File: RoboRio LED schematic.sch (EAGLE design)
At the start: 5 parts

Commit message: Jordan - RoboRio LED fixed
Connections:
- removed net 6V: R1.2, ROBORIO_PWM.2
- removed net N$3: D2.A, R2.1
- new net N$2: R1.2
- new net N$4: D2.A, R2.2
- net N$1: now also ROBORIO_PWM.2; no longer D1.A
- net S: now also R2.1; no longer R2.2
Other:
- moved on the sheet: R1, R2
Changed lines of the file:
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@@
 <instance part="D1" gate="G$1" x="-12.7" y="60.96" rot="R90"/>
 <instance part="D2" gate="G$1" x="20.32" y="60.96" rot="R90"/>
-<instance part="R1" gate="G$1" x="-27.94" y="60.96" rot="R180"/>
-<instance part="R2" gate="G$1" x="5.08" y="60.96" rot="R180"/>
+<instance part="R1" gate="G$1" x="-27.94" y="60.96"/>
+<instance part="R2" gate="G$1" x="5.08" y="60.96"/>
 </instances>
 <busses>
 </busses>
 <nets>
-<net name="N$1" class="0">
-<segment>
-<pinref part="R1" gate="G$1" pin="1"/>
-<pinref part="D1" gate="G$1" pin="A"/>
-<wire x1="-22.86" y1="60.96" x2="-15.24" y2="60.96" width="0.1524" layer="91"/>
-</segment>
-</net>
 <net name="S" class="0">
 <segment>
-<pinref part="D1" gate="G$1" pin="C"/>
-<pinref part="R2" gate="G$1" pin="2"/>
-<wire x1="-7.62" y1="60.96" x2="-5.08" y2="60.96" width="0.1524" layer="91"/>
 <pinref part="ROBORIO_PWM" gate="J$1" pin="3"/>
-<wire x1="-5.08" y1="60.96" x2="0" y2="60.96" width="0.1524" layer="91"/>
 <wire x1="-45.72" y1="63.5" x2="-45.72" y2="68.58" width="0.1524" layer="91"/>
 <wire x1="-45.72" y1="68.58" x2="-5.08" y2="68.58" width="0.1524" layer="91"/>
+<pinref part="D1" gate="G$1" pin="C"/>
+<pinref part="R2" gate="G$1" pin="1"/>
+<wire x1="-7.62" y1="60.96" x2="-5.08" y2="60.96" width="0.1524" layer="91"/>
+<wire x1="-5.08" y1="60.96" x2="0" y2="60.96" width="0.1524" layer="91"/>
 <wire x1="-5.08" y1="68.58" x2="-5.08" y2="60.96" width="0.1524" layer="91"/>
 <junction x="-5.08" y="60.96"/>
-</segment>
-</net>
-<net name="N$3" class="0">
-<segment>
-<pinref part="R2" gate="G$1" pin="1"/>
-<pinref part="D2" gate="G$1" pin="A"/>
-<wire x1="10.16" y1="60.96" x2="17.78" y2="60.96" width="0.1524" layer="91"/>
-</segment>
-</net>
-<net name="6V" class="0">
-<segment>
-<pinref part="ROBORIO_PWM" gate="J$1" pin="2"/>
-<pinref part="R1" gate="G$1" pin="2"/>
-<wire x1="-45.72" y1="60.96" x2="-33.02" y2="60.96" width="0.1524" layer="91"/>
 </segment>
 </net>
@@
 </segment>
 </net>
+<net name="N$1" class="0">
+<segment>
+<pinref part="ROBORIO_PWM" gate="J$1" pin="2"/>
+<pinref part="R1" gate="G$1" pin="1"/>
+<wire x1="-45.72" y1="60.96" x2="-33.02" y2="60.96" width="0.1524" layer="91"/>
+</segment>
+</net>
+<net name="N$2" class="0">
+<segment>
+<pinref part="R1" gate="G$1" pin="2"/>
+<wire x1="-22.86" y1="60.96" x2="-12.7" y2="60.96" width="0.1524" layer="91"/>
+</segment>
+</net>
+<net name="N$4" class="0">
+<segment>
+<pinref part="R2" gate="G$1" pin="2"/>
+<pinref part="D2" gate="G$1" pin="A"/>
+<wire x1="10.16" y1="60.96" x2="17.78" y2="60.96" width="0.1524" layer="91"/>
+</segment>
+</net>

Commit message: Jordan RoboRio LED Final
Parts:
- added D10, D11, D12, D13, D14, D15, D16, D17, D18, D19, D20, D3, D4, D5, D6, D7, D8, D9: (no value), SparkFun-LED:LED5MM
- added R10, R11, R12, R13, R14, R15, R16, R17, R18, R19, R20, R3, R4, R5, R6, R7, R8, R9: (no value), SparkFun-Passives:RESISTOR1206
- added ROBORIO_PWM1, ROBORIO_PWM2, ROBORIO_PWM3, ROBORIO_PWM4, ROBORIO_PWM5, ROBORIO_PWM6, ROBORIO_PWM7, ROBORIO_PWM8, ROBORIO_PWM9: (no value), SparkFun-Connectors:M03POGO_PIN_HOLES_ONLY
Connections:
- new net GND1: D4.C, ROBORIO_PWM1.1
- new net GND2: D6.C, ROBORIO_PWM2.1
- new net GND3: D8.C, ROBORIO_PWM3.1
- new net GND4: D10.C, ROBORIO_PWM4.1
- new net GND5: D12.C, ROBORIO_PWM5.1
- new net GND6: D14.C, ROBORIO_PWM6.1
- new net GND7: D16.C, ROBORIO_PWM7.1
- new net GND8: D18.C, ROBORIO_PWM8.1
- new net GND9: D20.C, ROBORIO_PWM9.1
- new net N$10: R7.1, ROBORIO_PWM3.2
- new net N$11: D7.A, R7.2
- new net N$12: D8.A, R8.2
- new net N$13: R9.1, ROBORIO_PWM4.2
- new net N$14: D9.A, R9.2
- new net N$15: D10.A, R10.2
- new net N$16: R11.1, ROBORIO_PWM5.2
- new net N$17: D11.A, R11.2
- new net N$18: D12.A, R12.2
- new net N$19: R13.1, ROBORIO_PWM6.2
- new net N$20: D13.A, R13.2
- new net N$21: D14.A, R14.2
- new net N$22: R15.1, ROBORIO_PWM7.2
- new net N$23: D15.A, R15.2
- new net N$24: D16.A, R16.2
- new net N$25: R17.1, ROBORIO_PWM8.2
- new net N$26: D17.A, R17.2
- new net N$27: D18.A, R18.2
- new net N$28: R19.1, ROBORIO_PWM9.2
- new net N$29: D19.A, R19.2
- new net N$3: R3.1, ROBORIO_PWM1.2
- new net N$30: D20.A, R20.2
- new net N$5: D3.A, R3.2
- new net N$6: D4.A, R4.2
- new net N$7: R5.1, ROBORIO_PWM2.2
- new net N$8: D5.A, R5.2
- new net N$9: D6.A, R6.2
- new net S1: D3.C, R4.1, ROBORIO_PWM1.3
- new net S2: D5.C, R6.1, ROBORIO_PWM2.3
- new net S3: D7.C, R8.1, ROBORIO_PWM3.3
- new net S4: D9.C, R10.1, ROBORIO_PWM4.3
- new net S5: D11.C, R12.1, ROBORIO_PWM5.3
- new net S6: D13.C, R14.1, ROBORIO_PWM6.3
- new net S7: D15.C, R16.1, ROBORIO_PWM7.3
- new net S8: D17.C, R18.1, ROBORIO_PWM8.3
- new net S9: D19.C, R20.1, ROBORIO_PWM9.3
- net N$2: now also D1.A
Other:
- moved on the sheet: D1, D2, R1, R2, ROBORIO_PWM

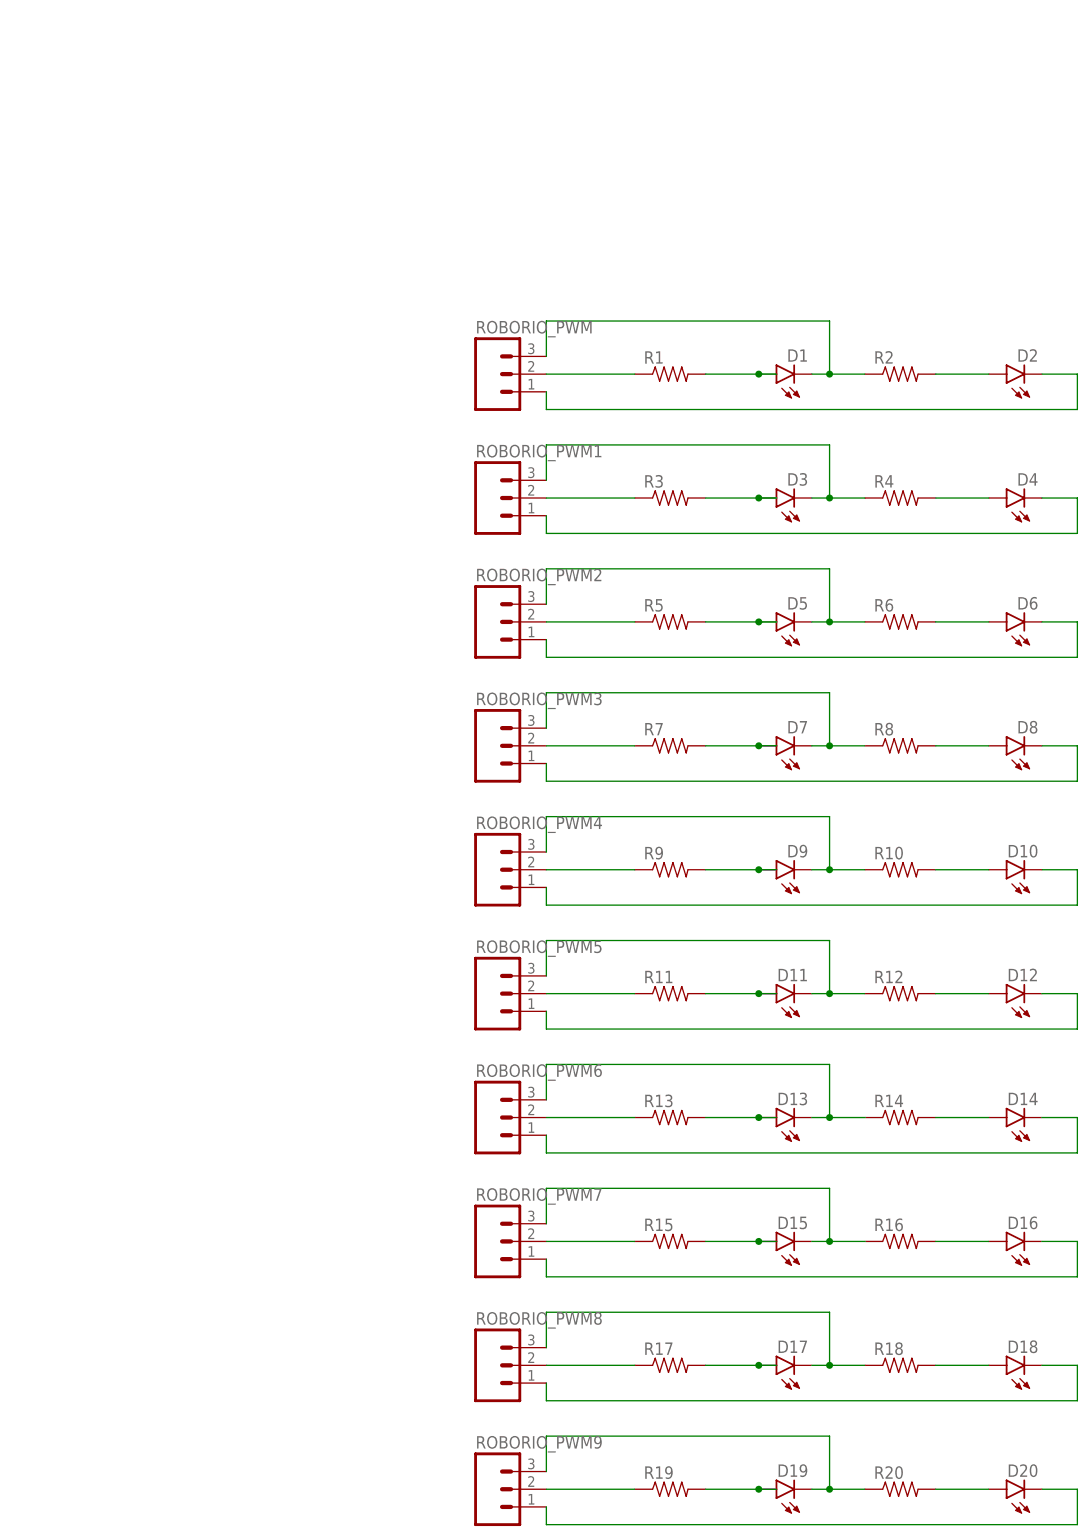
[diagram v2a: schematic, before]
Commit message: Advanced Electrical Project - Jordan Kiel - Surface Mount RoboRio LED
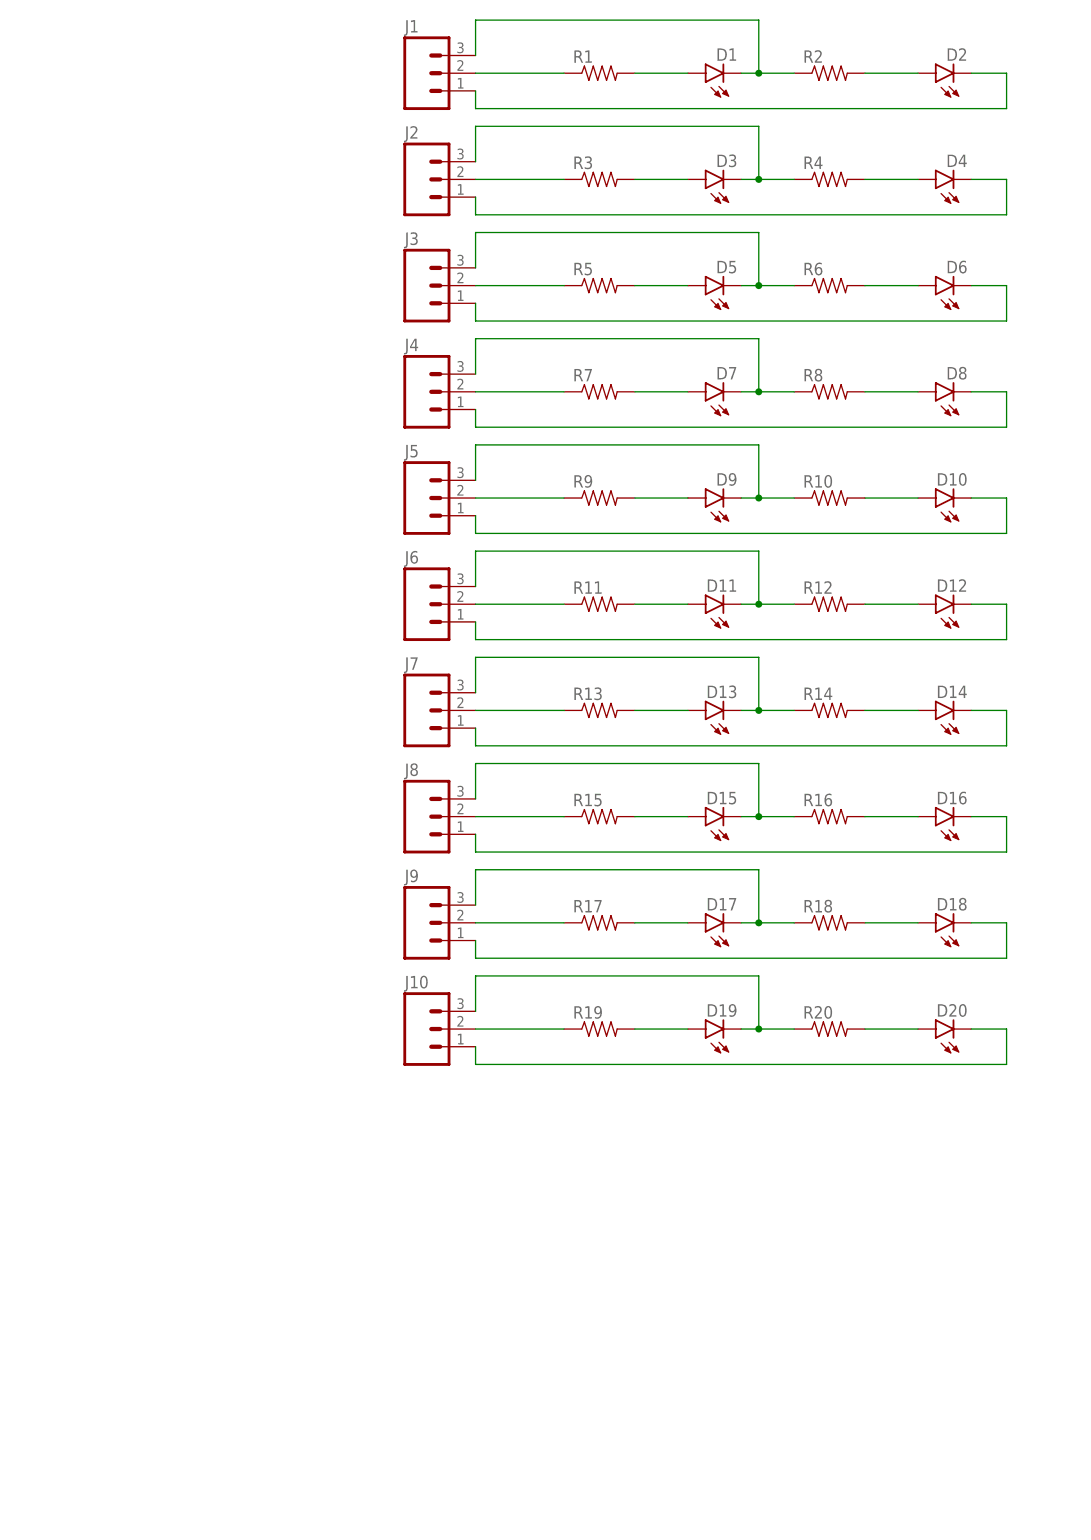
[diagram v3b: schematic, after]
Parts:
- removed ROBORIO_PWM, ROBORIO_PWM1, ROBORIO_PWM2, ROBORIO_PWM3, ROBORIO_PWM4, ROBORIO_PWM5, ROBORIO_PWM6, ROBORIO_PWM7, ROBORIO_PWM8, ROBORIO_PWM9: (no value), SparkFun-Connectors:M03POGO_PIN_HOLES_ONLY
- added J1, J10, J2, J3, J4, J5, J6, J7, J8, J9: (no value), SparkFun-Connectors:M03PTH
- D1, D10, D11, D12, D13, D14, D15, D16, D17, D18, D19, D2, D20, D3, D4, D5, D6, D7, D8, D9: device SparkFun-LED:LED5MM -> SparkFun-LED:LED1206
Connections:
- net GND: now also J1.1; no longer ROBORIO_PWM.1
- net GND1: now also J2.1; no longer ROBORIO_PWM1.1
- net GND2: now also J3.1; no longer ROBORIO_PWM2.1
- net GND3: now also J4.1; no longer ROBORIO_PWM3.1
- net GND4: now also J5.1; no longer ROBORIO_PWM4.1
- net GND5: now also J6.1; no longer ROBORIO_PWM5.1
- net GND6: now also J7.1; no longer ROBORIO_PWM6.1
- net GND7: now also J8.1; no longer ROBORIO_PWM7.1
- net GND8: now also J9.1; no longer ROBORIO_PWM8.1
- net GND9: now also J10.1; no longer ROBORIO_PWM9.1
- net N$1: now also J1.2; no longer ROBORIO_PWM.2
- net N$10: now also J4.2; no longer ROBORIO_PWM3.2
- net N$13: now also J5.2; no longer ROBORIO_PWM4.2
- net N$16: now also J6.2; no longer ROBORIO_PWM5.2
- net N$19: now also J7.2; no longer ROBORIO_PWM6.2
- net N$22: now also J8.2; no longer ROBORIO_PWM7.2
- net N$25: now also J9.2; no longer ROBORIO_PWM8.2
- net N$28: now also J10.2; no longer ROBORIO_PWM9.2
- net N$3: now also J2.2; no longer ROBORIO_PWM1.2
- net N$7: now also J3.2; no longer ROBORIO_PWM2.2
- net S: now also J1.3; no longer ROBORIO_PWM.3
- net S1: now also J2.3; no longer ROBORIO_PWM1.3
- net S2: now also J3.3; no longer ROBORIO_PWM2.3
- net S3: now also J4.3; no longer ROBORIO_PWM3.3
- net S4: now also J5.3; no longer ROBORIO_PWM4.3
- net S5: now also J6.3; no longer ROBORIO_PWM5.3
- net S6: now also J7.3; no longer ROBORIO_PWM6.3
- net S7: now also J8.3; no longer ROBORIO_PWM7.3
- net S8: now also J9.3; no longer ROBORIO_PWM8.3
- net S9: now also J10.3; no longer ROBORIO_PWM9.3
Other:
- moved on the sheet: D1, D10, D11, D12, D13, D14, D15, D16, D17, D18, D19, D2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
